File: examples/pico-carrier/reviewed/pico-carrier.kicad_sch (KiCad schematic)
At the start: 9 parts, among them J1 5V IN, J3 GP0-GP15, J4 GP16-GP28, PWR, U1 Pico

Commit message: Relieve the pads, fillet the joints, and give the board its screw holes
Three of the reviewer's manufacturing points, and they largely fall out
of the one before it - once KiCad fills the plane, the thermal relief it
was already asked for in the file actually appears.

**Thermal relief.** The zones said thermal all along; our own filler
ignored it and flooded every land solid. KiCad's does not, so every
through-hole ground pad now sits in a gap bridged by four spokes and an
iron can bring the joint up without heating a hundred square millimetres
of copper. `layout.solid_pad_connection` reports the setting when a
board turns it off: drilled pads only, because a surface pad reflows in
an oven that is heating the plane anyway and flooding it is often the
better thermal answer.

**Teardrops.** A track entering a land is a step change in width, and a
step change is where copper tears - the connector gets levered on and
off, the drill wanders, and the crack starts at the corner. `_teardrops`
replaces the first stretch of each run with a three-step taper into the
land, checked against its neighbours before it is kept, so a fillet
never eats the clearance a fine-pitch escape needs. It *replaces* rather
than overlays: laying the taper on top of the run drew the same copper
twice, and `route.acute_angle` reported all thirty of them, correctly.
`route.mixed_track_widths` learns what a fillet looks like so a properly
filleted board does not read as one nobody decided the width of.

**Mounting holes.** Four M3 holes near the corners, placed before the
router runs because they are obstacles, and slid along the edges or a
little inboard where a connector body has the corner - the motor board
and the op-amp take three, which is what those floorplans have room for.
Grounded on the motor driver, whose chassis is metal and part of the
shield, plain on the rest: bonding the enclosure to the reference is the
enclosure's decision, not the board's.

Two things that fell out of placing par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
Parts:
- added H1, H2, H3, H4: M33, MountingHole:MountingHole_3.2mm_M3, symbol Mechanical:MountingHole
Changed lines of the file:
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@@
     (instances (project "pico-carrier" (path "/f86b03a2-2f64-5dc5-a6a7-b575bc25ae3a" (reference "D3") (unit 1))))
+  )
+  (symbol (lib_id "Mechanical:MountingHole") (at 101.6 170.18 0.0) (unit 1)
+    (exclude_from_sim no) (in_bom yes) (on_board yes) (dnp no)
+    (property "Reference" "H1" (at 100.33 166.37 0) (effects (font (size 1.27 1.27)) (justify right)))
+    (property "Value" "M33" (at 105.41 172.72 0) (effects (font (size 1.27 1.27)) (justify left)))
+    (property "Footprint" "MountingHole:MountingHole_3.2mm_M3" (at 101.6 170.18 0) (effects (font (size 1.27 1.27)) hide))
+    (property "Datasheet" "~" (at 101.6 170.18 0) (effects (font (size 1.27 1.27)) hide))
+    (property "MPN" "n/a" (at 101.6 170.18 0) (effects (font (size 1.27 1.27)) hide))
+    (property "Manufacturer" "n/a" (at 101.6 170.18 0) (effects (font (size 1.27 1.27)) hide))
+    (instances (project "pico-carrier" (path "/f86b03a2-2f64-5dc5-a6a7-b575bc25ae3a" (reference "H1") (unit 1))))
+  )
+  (symbol (lib_id "Mechanical:MountingHole") (at 114.3 170.18 0.0) (unit 1)
+    (exclude_from_sim no) (in_bom yes) (on_board yes) (dnp no)
+    (property "Reference" "H2" (at 113.03 166.37 0) (effects (font (size 1.27 1.27)) (justify right)))
+    (property "Value" "M33" (at 118.11 172.72 0) (effects (font (size 1.27 1.27)) (justify left)))
+    (property "Footprint" "MountingHole:MountingHole_3.2mm_M3" (at 114.3 170.18 0) (effects (font (size 1.27 1.27)) hide))
+    (property "Datasheet" "~" (at 114.3 170.18 0) (effects (font (size 1.27 1.27)) hide))
+    (property "MPN" "n/a" (at 114.3 170.18 0) (effects (font (size 1.27 1.27)) hide))
+    (property "Manufacturer" "n/a" (at 114.3 170.18 0) (effects (font (size 1.27 1.27)) hide))
+    (instances (project "pico-carrier" (path "/f86b03a2-2f64-5dc5-a6a7-b575bc25ae3a" (reference "H2") (unit 1))))
+  )
+  (symbol (lib_id "Mechanical:MountingHole") (at 127.0 170.18 0.0) (unit 1)
+    (exclude_from_sim no) (in_bom yes) (on_board yes) (dnp no)
+    (property "Reference" "H3" (at 125.73 166.37 0) (effects (font (size 1.27 1.27)) (justify right)))
+    (property "Value" "M33" (at 130.81 172.72 0) (effects (font (size 1.27 1.27)) (justify left)))
+    (property "Footprint" "MountingHole:MountingHole_3.2mm_M3" (at 127.0 170.18 0) (effects (font (size 1.27 1.27)) hide))
+    (property "Datasheet" "~" (at 127.0 170.18 0) (effects (font (size 1.27 1.27)) hide))
+    (property "MPN" "n/a" (at 127.0 170.18 0) (effects (font (size 1.27 1.27)) hide))
+    (property "Manufacturer" "n/a" (at 127.0 170.18 0) (effects (font (size 1.27 1.27)) hide))
+    (instances (project "pico-carrier" (path "/f86b03a2-2f64-5dc5-a6a7-b575bc25ae3a" (reference "H3") (unit 1))))
+  )
+  (symbol (lib_id "Mechanical:MountingHole") (at 139.7 170.18 0.0) (unit 1)
+    (exclude_from_sim no) (in_bom yes) (on_board yes) (dnp no)
+    (property "Reference" "H4" (at 138.43 166.37 0) (effects (font (size 1.27 1.27)) (justify right)))
+    (property "Value" "M33" (at 143.51 172.72 0) (effects (font (size 1.27 1.27)) (justify left)))
+    (property "Footprint" "MountingHole:MountingHole_3.2mm_M3" (at 139.7 170.18 0) (effects (font (size 1.27 1.27)) hide))
+    (property "Datasheet" "~" (at 139.7 170.18 0) (effects (font (size 1.27 1.27)) hide))
+    (property "MPN" "n/a" (at 139.7 170.18 0) (effects (font (size 1.27 1.27)) hide))
+    (property "Manufacturer" "n/a" (at 139.7 170.18 0) (effects (font (size 1.27 1.27)) hide))
+    (instances (project "pico-carrier" (path "/f86b03a2-2f64-5dc5-a6a7-b575bc25ae3a" (reference "H4") (unit 1))))
   )
   (wire (pts (xy 180.34 107.95) (xy 180.34 105.41)) (stroke (width 0) (type default)))

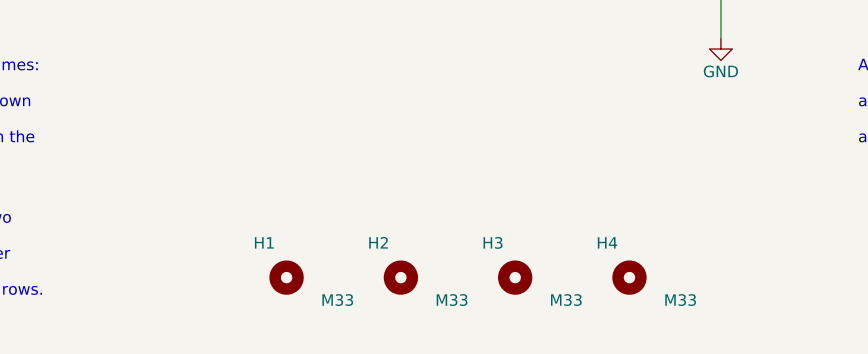
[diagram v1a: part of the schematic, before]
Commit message: Give the assembly machine something to aim at
Fiducials: three copper dots in bare mask windows, near three different
corners so a pick-and-place gets rotation as well as offset. It aligns
to the board, not to the drawing - without them it has only the routed
outline, cut to a tolerance ten times looser than the placement a 0.5 mm
pitch part is asking for. `fab.no_fiducials` reports a fine-pitch board
that has none, as context rather than as a fault: plenty of boards are
built one at a time with tweezers.

They share the corner search with the mounting holes, which is where
this found a real bug: `_courtyard_box` read lines and rectangles only,
and a mounting hole draws its courtyard as one circle - so every hole
measured as taking up no room at all, and the first three fiducials
landed on top of three screw holes. Circles and arcs count now.

Co-Authored-By: Claude Fable 5 <noreply@anthropic.com>
Claude-Session: https://claude.ai/code/session_01DUj7Ltu92tWg159mCSacwY
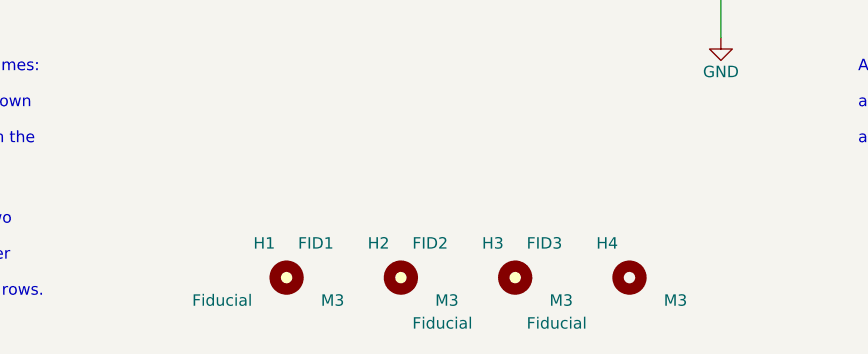
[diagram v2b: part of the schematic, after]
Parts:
- added FID1, FID2, FID3: Fiducial, Fiducial:Fiducial_1mm_Mask2mm, symbol Mechanical:Fiducial
- H1, H2, H3, H4: value M33 -> M3
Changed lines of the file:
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@@
     (exclude_from_sim no) (in_bom yes) (on_board yes) (dnp no)
     (property "Reference" "H1" (at 100.33 166.37 0) (effects (font (size 1.27 1.27)) (justify right)))
-    (property "Value" "M33" (at 105.41 172.72 0) (effects (font (size 1.27 1.27)) (justify left)))
+    (property "Value" "M3" (at 105.41 172.72 0) (effects (font (size 1.27 1.27)) (justify left)))
     (property "Footprint" "MountingHole:MountingHole_3.2mm_M3" (at 101.6 170.18 0) (effects (font (size 1.27 1.27)) hide))
     (property "Datasheet" "~" (at 101.6 170.18 0) (effects (font (size 1.27 1.27)) hide))
@@
     (exclude_from_sim no) (in_bom yes) (on_board yes) (dnp no)
     (property "Reference" "H2" (at 113.03 166.37 0) (effects (font (size 1.27 1.27)) (justify right)))
-    (property "Value" "M33" (at 118.11 172.72 0) (effects (font (size 1.27 1.27)) (justify left)))
+    (property "Value" "M3" (at 118.11 172.72 0) (effects (font (size 1.27 1.27)) (justify left)))
     (property "Footprint" "MountingHole:MountingHole_3.2mm_M3" (at 114.3 170.18 0) (effects (font (size 1.27 1.27)) hide))
     (property "Datasheet" "~" (at 114.3 170.18 0) (effects (font (size 1.27 1.27)) hide))
@@
     (exclude_from_sim no) (in_bom yes) (on_board yes) (dnp no)
     (property "Reference" "H3" (at 125.73 166.37 0) (effects (font (size 1.27 1.27)) (justify right)))
-    (property "Value" "M33" (at 130.81 172.72 0) (effects (font (size 1.27 1.27)) (justify left)))
+    (property "Value" "M3" (at 130.81 172.72 0) (effects (font (size 1.27 1.27)) (justify left)))
     (property "Footprint" "MountingHole:MountingHole_3.2mm_M3" (at 127.0 170.18 0) (effects (font (size 1.27 1.27)) hide))
     (property "Datasheet" "~" (at 127.0 170.18 0) (effects (font (size 1.27 1.27)) hide))
@@
     (exclude_from_sim no) (in_bom yes) (on_board yes) (dnp no)
     (property "Reference" "H4" (at 138.43 166.37 0) (effects (font (size 1.27 1.27)) (justify right)))
-    (property "Value" "M33" (at 143.51 172.72 0) (effects (font (size 1.27 1.27)) (justify left)))
+    (property "Value" "M3" (at 143.51 172.72 0) (effects (font (size 1.27 1.27)) (justify left)))
     (property "Footprint" "MountingHole:MountingHole_3.2mm_M3" (at 139.7 170.18 0) (effects (font (size 1.27 1.27)) hide))
     (property "Datasheet" "~" (at 139.7 170.18 0) (effects (font (size 1.27 1.27)) hide))
@@
     (instances (project "pico-carrier" (path "/f86b03a2-2f64-5dc5-a6a7-b575bc25ae3a" (reference "H4") (unit 1))))
   )
+  (symbol (lib_id "Mechanical:Fiducial") (at 101.6 170.18 0.0) (unit 1)
+    (exclude_from_sim no) (in_bom yes) (on_board yes) (dnp no)
+    (property "Reference" "FID1" (at 102.87 166.37 0) (effects (font (size 1.27 1.27)) (justify left)))
+    (property "Value" "Fiducial" (at 97.79 172.72 0) (effects (font (size 1.27 1.27)) (justify right)))
+    (property "Footprint" "Fiducial:Fiducial_1mm_Mask2mm" (at 101.6 170.18 0) (effects (font (size 1.27 1.27)) hide))
+    (property "Datasheet" "~" (at 101.6 170.18 0) (effects (font (size 1.27 1.27)) hide))
+    (property "MPN" "n/a" (at 101.6 170.18 0) (effects (font (size 1.27 1.27)) hide))
+    (property "Manufacturer" "n/a" (at 101.6 170.18 0) (effects (font (size 1.27 1.27)) hide))
+    (instances (project "pico-carrier" (path "/f86b03a2-2f64-5dc5-a6a7-b575bc25ae3a" (reference "FID1") (unit 1))))
+  )
+  (symbol (lib_id "Mechanical:Fiducial") (at 114.3 170.18 0.0) (unit 1)
+    (exclude_from_sim no) (in_bom yes) (on_board yes) (dnp no)
+    (property "Reference" "FID2" (at 115.57 166.37 0) (effects (font (size 1.27 1.27)) (justify left)))
+    (property "Value" "Fiducial" (at 115.57 175.26 0) (effects (font (size 1.27 1.27)) (justify left)))
+    (property "Footprint" "Fiducial:Fiducial_1mm_Mask2mm" (at 114.3 170.18 0) (effects (font (size 1.27 1.27)) hide))
+    (property "Datasheet" "~" (at 114.3 170.18 0) (effects (font (size 1.27 1.27)) hide))
+    (property "MPN" "n/a" (at 114.3 170.18 0) (effects (font (size 1.27 1.27)) hide))
+    (property "Manufacturer" "n/a" (at 114.3 170.18 0) (effects (font (size 1.27 1.27)) hide))
+    (instances (project "pico-carrier" (path "/f86b03a2-2f64-5dc5-a6a7-b575bc25ae3a" (reference "FID2") (unit 1))))
+  )
+  (symbol (lib_id "Mechanical:Fiducial") (at 127.0 170.18 0.0) (unit 1)
+    (exclude_from_sim no) (in_bom yes) (on_board yes) (dnp no)
+    (property "Reference" "FID3" (at 128.27 166.37 0) (effects (font (size 1.27 1.27)) (justify left)))
+    (property "Value" "Fiducial" (at 128.27 175.26 0) (effects (font (size 1.27 1.27)) (justify left)))
+    (property "Footprint" "Fiducial:Fiducial_1mm_Mask2mm" (at 127.0 170.18 0) (effects (font (size 1.27 1.27)) hide))
+    (property "Datasheet" "~" (at 127.0 170.18 0) (effects (font (size 1.27 1.27)) hide))
+    (property "MPN" "n/a" (at 127.0 170.18 0) (effects (font (size 1.27 1.27)) hide))
+    (property "Manufacturer" "n/a" (at 127.0 170.18 0) (effects (font (size 1.27 1.27)) hide))
+    (instances (project "pico-carrier" (path "/f86b03a2-2f64-5dc5-a6a7-b575bc25ae3a" (reference "FID3") (unit 1))))
+  )
   (wire (pts (xy 180.34 107.95) (xy 180.34 105.41)) (stroke (width 0) (type default)))

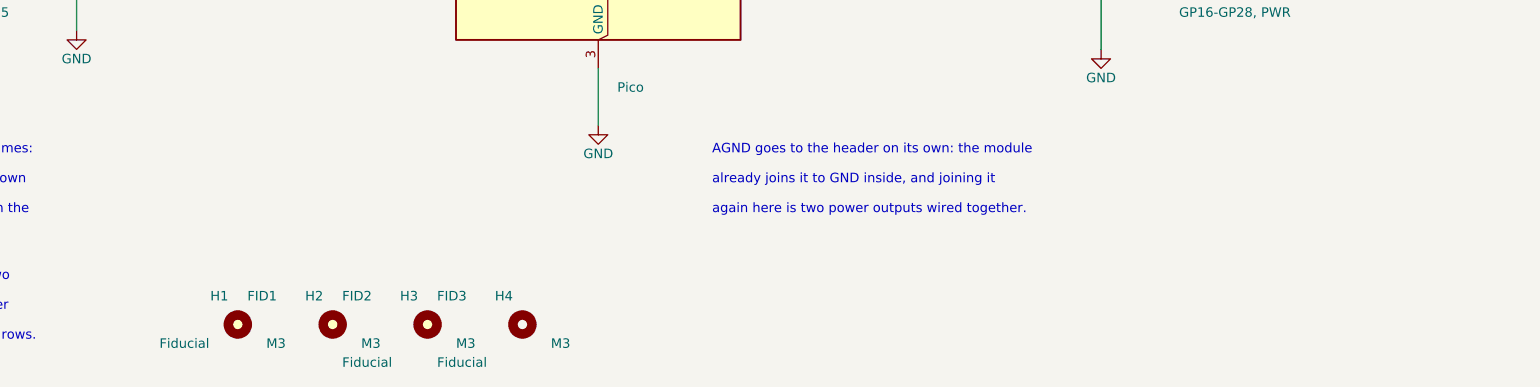
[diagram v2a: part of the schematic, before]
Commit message: Let the new parts sit somewhere sensible, on the board and on the sheet
Placing screw holes and fiducials turned up four things that were wrong
before either existed, all of them about where something is allowed to
go rather than about the parts themselves.

A designator was kept off the pads but not inside the board outline, so
any part at the edge - a connector, and now a hole - had its reference
clipped by the edge. Every board had been carrying one or two of those.

A symbol with no pins leaves no trace in the sheet planner's obstacle
list, because that list is built from pin stubs. The screw holes were
invisible to it and the fiducials landed on top of them. The free-row
search also ran off the right-hand edge of an A4 page and sat over the
title block on the way, which is `readability.outside_page` and
`readability.margin_intrusion` respectively - both real, both now
avoided by bounding the search to the drawing area.

And the bill-of-materials flag is read from the footprint rather than
the symbol library, because the footprint is the side KiCad's parity
check reads and the side the fab agrees with. That retired three
warnings the op-amp board had been carrying since it gained test
points: `Connector:TestPoint` claims to be a BOM line and its own
footprint says otherwise.

All four fast boards pass their gates; the suite is green on 10.0.4.

Co-Authored-By: Claude Fable 5 <noreply@anthropic.com>
Claude-Session: https://claude.ai/code/session_01DUj7Ltu92tWg159mCSacwY
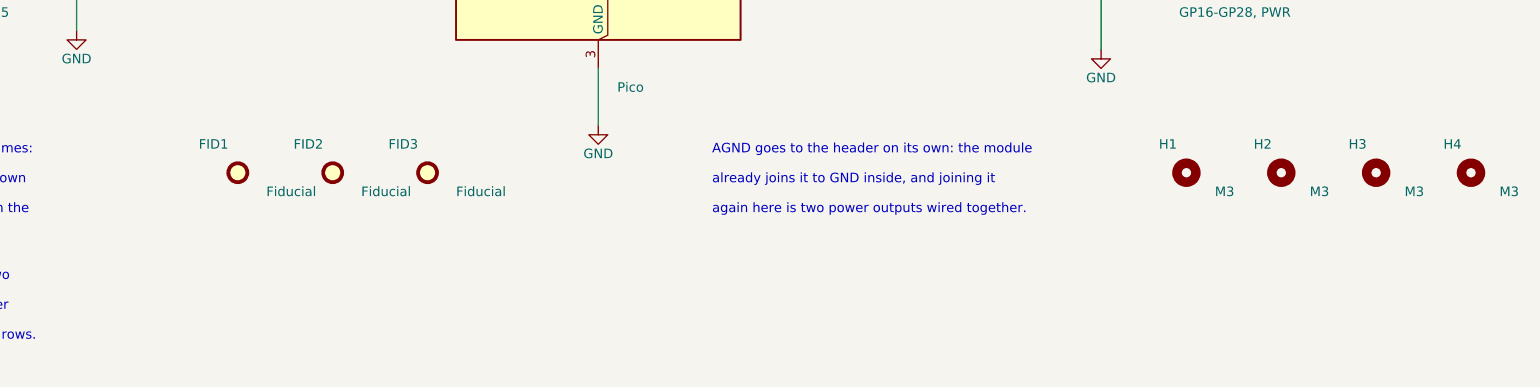
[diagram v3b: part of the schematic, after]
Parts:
- FID1, FID2, FID3, H1, H2, H3, H4: now left out of the parts list
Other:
- moved on the sheet: FID1, FID2, FID3, H1, H2, H3, H4
